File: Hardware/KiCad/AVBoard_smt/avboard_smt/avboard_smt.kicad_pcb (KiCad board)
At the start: 4 copper layers, 177 x 152.1 mm, 121 parts, among them IC1 AS7C256A-10TIN, IC2 IS61C64AL-10TLI, IC2_AUD0 7432N, IC3 SN74CBT16210CDLR, IC36 4040N, IC37 7430N, IC39 7400N, IC4 74VHC157FT, IC40 4040N, IC41 7400N, IC43 7400N, IC44 7486N, IC45 7400N, IC46 74257N, IC47 74257N, IC48 74564N, IC4_AUD0 7400N, IC53 7404N, IC6_AUD0 7474N, IC7_AUD0 LM358N, IC9 AS7C256A-10TIN, J1 5V, J2 VID_TO_MOBO, U1 W65C02SP, U10 74AHC373, U2 THS7374, U3 74AHC373, U4 74AHC373, U5 74AHC373, U6 74AC00, U7 74VHC74, U8 74HC244, U9 74HC244

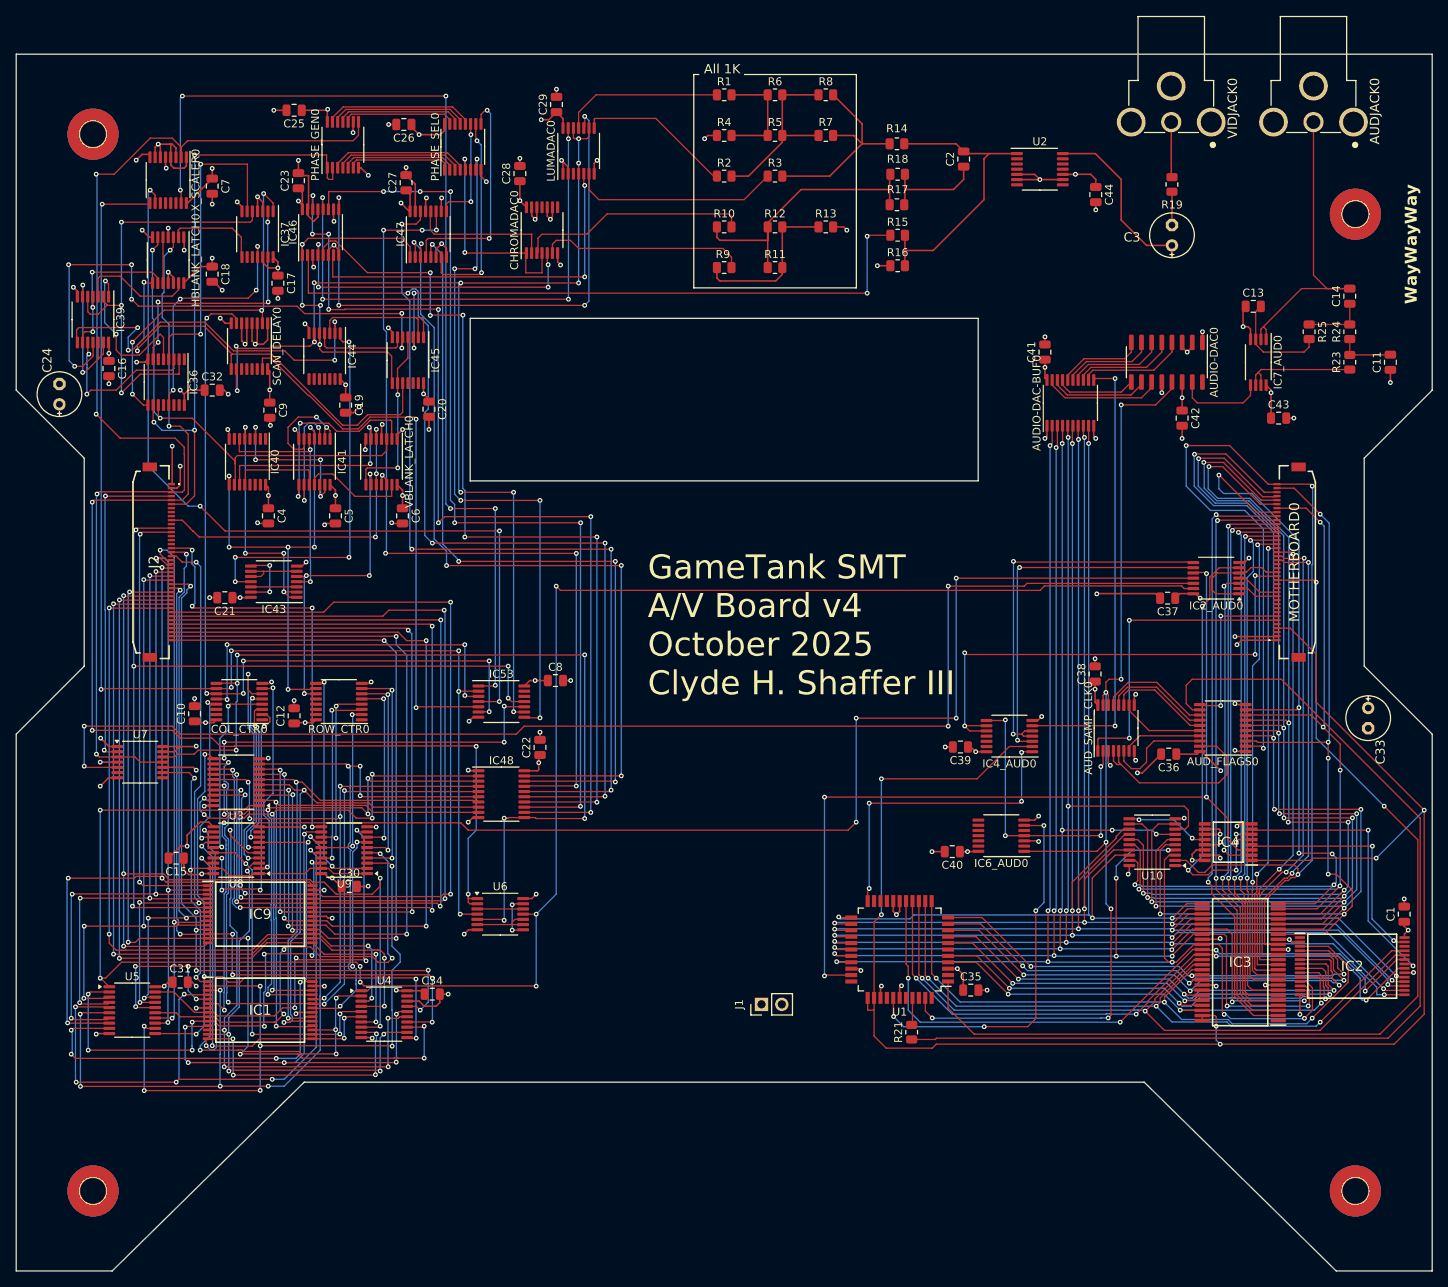
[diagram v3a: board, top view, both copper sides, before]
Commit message: Add AV board version with VRAM replaced but not ARAM
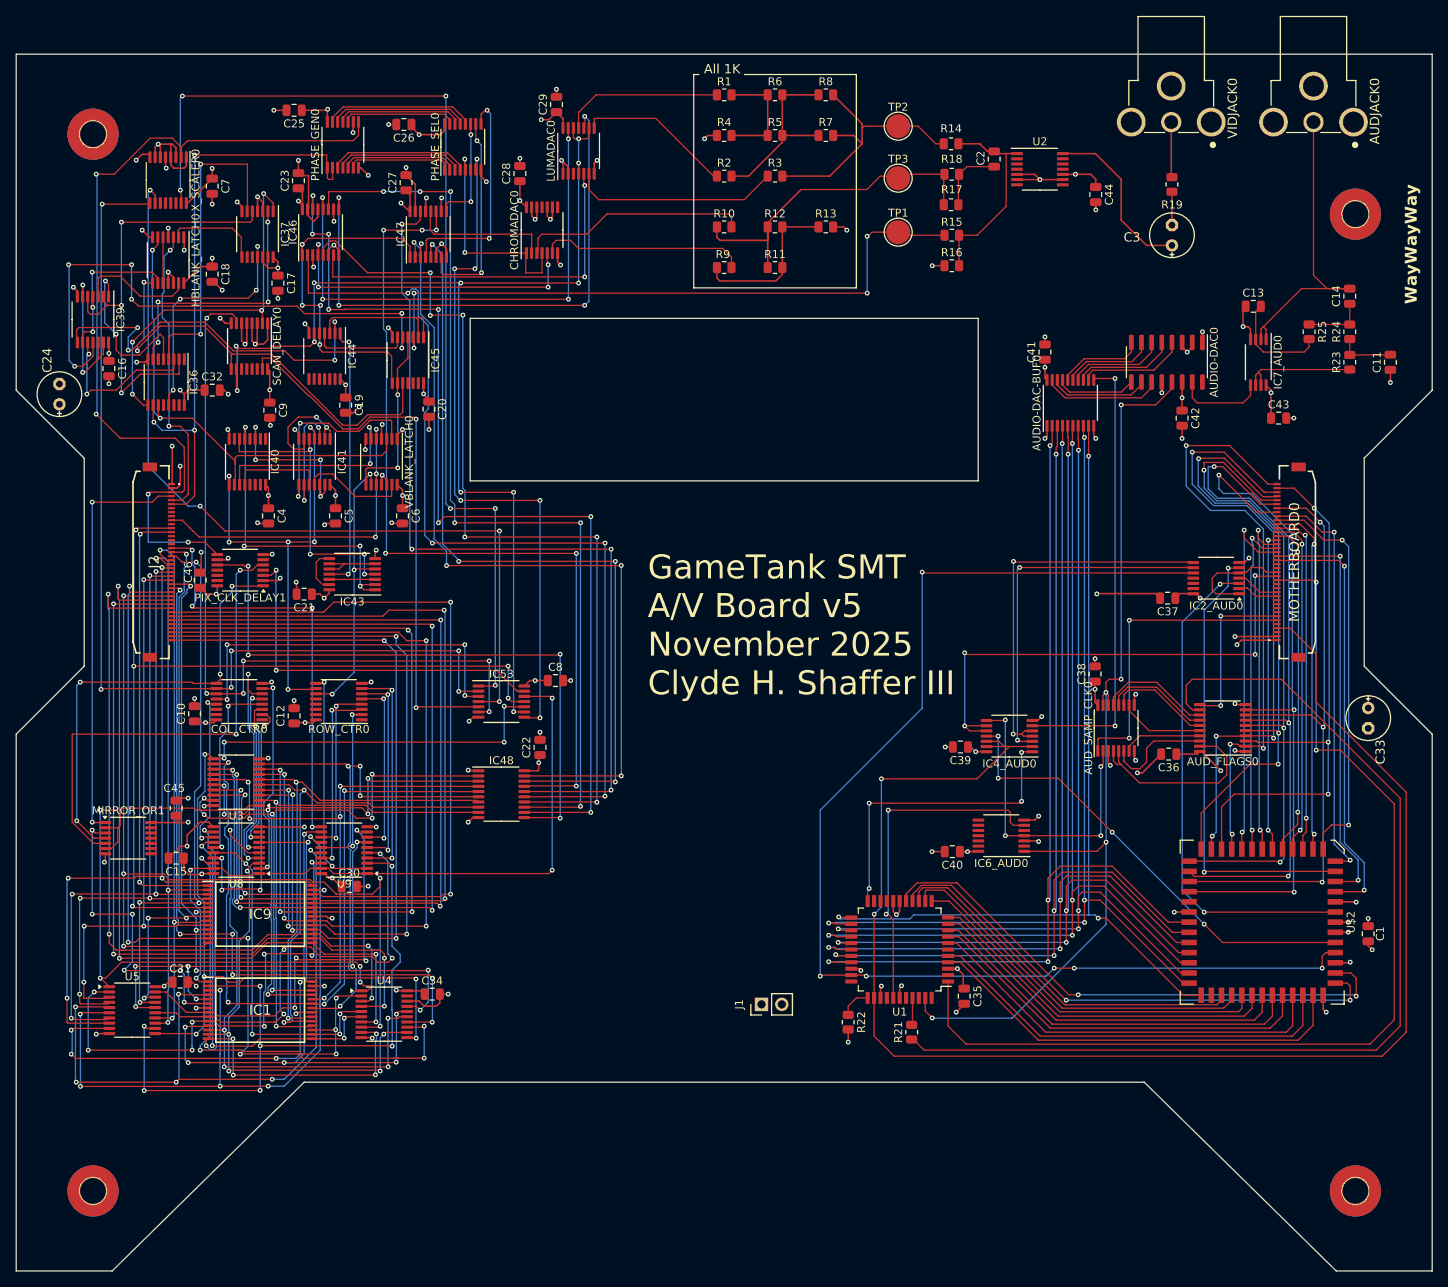
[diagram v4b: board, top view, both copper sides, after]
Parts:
- removed IC2: IS61C64AL-10TLI, SamacSys_Parts:SOP55P1340X120-28N
- removed IC3: SN74CBT16210CDLR, SamacSys_Parts:SOP64P1035X279-48N
- removed IC4: 74VHC157FT, SamacSys_Parts:SOP65P640X120-16N
- removed U10: 74AHC373, Package_SO:TSSOP-20_4.4x6.5mm_P0.65mm
- removed U6: 74AC00, Package_SO:TSSOP-14_4.4x5mm_P0.65mm
- removed U7: 74VHC74, Package_SO:TSSOP-14_4.4x5mm_P0.65mm
- added C45: 0.1uF, Capacitor_SMD:C_0805_2012Metric, F.Cu at (80.0, 135.8)
- added C46: 0.1uF, Capacitor_SMD:C_0805_2012Metric, F.Cu at (83.0, 107.2)
- added MIRROR_OR1: 7432N, Package_SO:TSSOP-14_4.4x5mm_P0.65mm, F.Cu at (74.0, 139.5)
- added PIX_CLK_DELAY1: 74164N, Package_SO:TSSOP-14_4.4x5mm_P0.65mm, F.Cu at (88.0, 106.0)
- added R22: 3.3k, Resistor_SMD:R_0805_2012Metric, F.Cu at (164.0, 162.5)
- added TP1: Sync, TestPoint:TestPoint_Pad_D3.0mm, F.Cu at (170.2, 63.8)
- added TP2: Luma, TestPoint:TestPoint_Pad_D3.0mm, F.Cu at (170.2, 50.5)
- added TP3: Chroma, TestPoint:TestPoint_Pad_D3.0mm, F.Cu at (170.2, 57.0)
- added U$2: PDPRAM_4KPLCC52S, Package_LCC:PLCC-52, F.Cu at (215.8, 150.0)
- moved C21 9.93 mm to (96.0, 109.0)
- moved IC43 9.84 mm to (102.0, 106.5)
- moved R14 6.77 mm to (176.9, 52.7)
- moved R15 6.77 mm to (176.9, 64.1)
- moved R16 6.77 mm to (176.9, 67.9)
- moved R17 6.77 mm to (176.9, 60.3)
- moved R18 6.77 mm to (176.9, 56.5)
- moved C1 5.12 mm to (229.0, 151.4)
- moved C2 3.81 mm to (182.2, 54.6)
- moved C35 1.12 mm to (178.5, 159.2), turned to -90 degrees
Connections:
- net Net-(COL_CTR0A-Q9) renamed /Composite Video Generator/ROW_COMPLETE
- COL_CTR0 pad 9: /Composite Video Generator/PIXLATCH -> /Composite Video Generator/PIXCLK
- IC1 pad 1: Net-(IC1-~{OE}) -> /Composite Video Generator/~{PIXLOAD}
- IC2_AUD0 pad 11: /Composite Video Generator/~{MirrorWE} -> (no net)
- IC2_AUD0 pad 12: /Composite Video Generator/LAG14 -> (no net)
- IC2_AUD0 pad 13: /Composite Video Generator/~{MirrorLoad} -> (no net)
- IC2_AUD0 pad 3: /signals_4/Sys_ARAM_~{WE} -> Net-(IC2_AUD0A-O)
- IC2_AUD0 pad 6: /signals_4/Sys_ARAM_~{OE} -> Net-(IC2_AUD0B-O)
- IC4_AUD0 pad 11: unconnected-(IC4_AUD0D-O-Pad11) -> Net-(IC4_AUD0D-O)
- IC4_AUD0 pad 12: unconnected-(IC4_AUD0D-I0-Pad12) -> /signals_4/CLK14_AUD
- IC4_AUD0 pad 13: unconnected-(IC4_AUD0D-I1-Pad13) -> /signals_4/CLK14_AUD
- IC53 pad 12: (no net) -> /Composite Video Generator/~{PIXLOAD}
- IC53 pad 13: (no net) -> /Composite Video Generator/PIXLOAD
- U1 pad 36: /signals_4/CLK14_AUD -> Net-(U1-BE)
- U8 pad 1: Net-(IC1-~{OE}) -> /Composite Video Generator/~{PIXLOAD}
- U8 pad 19: Net-(IC1-~{OE}) -> /Composite Video Generator/~{PIXLOAD}
- U9 pad 1: Net-(IC1-~{OE}) -> /Composite Video Generator/~{PIXLOAD}
- U9 pad 19: Net-(IC1-~{OE}) -> /Composite Video Generator/~{PIXLOAD}
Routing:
- net /Composite Video Generator/LAG14: track 166.3 -> 0.00 mm, vias 4 -> 0
- net /Composite Video Generator/~{MirrorLoad}: track 235.0 -> 89.4 mm, vias 7 -> 4
- net /Composite Video Generator/~{MirrorWE}: track 178.7 -> 38.9 mm
- net /Composite Video Generator/CLK7: track 147.0 -> 37.3 mm, vias 6 -> 2
- net /Composite Video Generator/~{PIXLOAD}: track 0.00 -> 87.4 mm, vias 0 -> 4
- net Net-(AUD_FLAGS0A-1D): track 143.9 -> 75.4 mm
- net Net-(IC2_AUD0A-O): track 0.00 -> 62.9 mm, vias 0 -> 2
- net /Composite Video Generator/PIXCLK_PhaseC: track 0.00 -> 60.6 mm, vias 0 -> 2
- net Net-(IC4_AUD0D-O): track 0.00 -> 57.4 mm, vias 0 -> 4
- net Net-(IC2_AUD0B-O): track 0.00 -> 57.0 mm, vias 0 -> 2
- net Net-(AUD_FLAGS0A-3D): track 133.8 -> 76.8 mm, vias 6 -> 4
- net Net-(AUD_FLAGS0A-4D): track 133.9 -> 77.4 mm, vias 6 -> 3
- net /Composite Video Generator/PIXCLK: track 0.00 -> 55.9 mm, vias 0 -> 4
- net /signals_4/Sys_ARAM_~{OE}: track 55.8 -> 0.00 mm, vias 4 -> 0
- net Net-(IC1-~{OE}): track 54.8 -> 0.00 mm, vias 3 -> 0
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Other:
- board text added: "GameTank SMT A/V Board v5 November 2025 Clyde H. Shaffer III"
- board text removed: "GameTank SMT A/V Board v4 October 2025 Clyde H. Shaffer III"
